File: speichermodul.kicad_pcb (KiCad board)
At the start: 2 copper layers, 100 x 160 mm, 69 parts, among them IC1 6116, J1 2PinTerminalBlocktg, J2 2PinTerminalBlocktg, J3 2PinTerminalBlocktg, P1 CONN_3X2, P8 CONN_02X10, P9 CONN_02X10, SW1 SW_PUSH-tg, SW2 SW_PUSH-tg, U1 7400, U2 74LS08, U3 74LS08, U4 74LS14, U5 74LS540, U6 74LS540

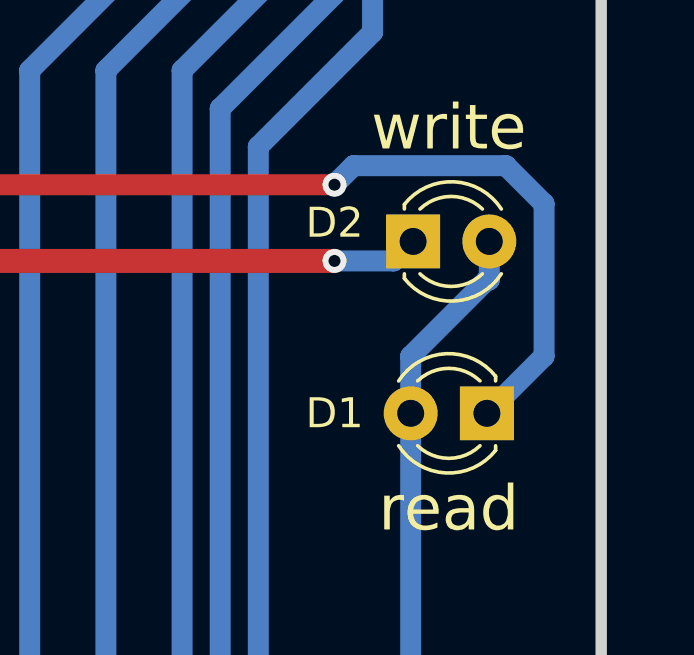
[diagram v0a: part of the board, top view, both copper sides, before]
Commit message: LEDs richtig rum gedreht
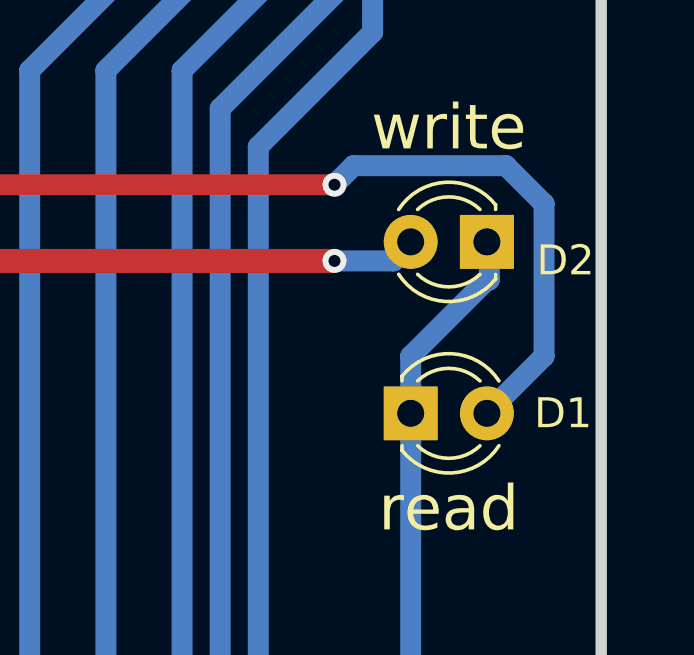
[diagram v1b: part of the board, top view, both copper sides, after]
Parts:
- moved D1 2.54 mm to (121.9, 125.7), turned to 0 degrees
- moved D2 2.46 mm to (124.5, 120.0), turned to 180 degrees
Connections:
- D1 pad 1: Net-(D1-Pad1) -> GND
- D1 pad 2: GND -> Net-(D1-Pad2)
- D2 pad 1: Net-(D2-Pad1) -> GND
- D2 pad 2: GND -> Net-(D2-Pad2)
- R7 pad 2: Net-(D1-Pad1) -> Net-(D1-Pad2)
- R8 pad 2: Net-(D2-Pad1) -> Net-(D2-Pad2)
- RP1 pad 5: (no net) -> Net-(RP1-Pad5)
- SW1 pad 2: (no net) -> Net-(SW1-Pad2)
- SW2 pad 2: (no net) -> Net-(SW2-Pad2)
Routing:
- net Net-(D1-Pad2): track 0.00 -> 65.5 mm, vias 0 -> 2
- net Net-(D1-Pad1): track 65.5 -> 0.00 mm, vias 2 -> 0
- net Net-(D2-Pad2): track 0.00 -> 57.7 mm, vias 0 -> 2
- net Net-(D2-Pad1): track 57.7 -> 0.00 mm, vias 2 -> 0

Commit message: Speichermodul weitergebaut
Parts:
- removed G***: LOGO, allBonsaiFootprintsLibs:agi5

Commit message: Speicher weitergebaut
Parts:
- removed RP2: R_PACK8BUSSED, Housings_SIP:SIP9_Housing_BigPads
- added C8: CP, Capacitor_THT:CP_Radial_D8.0mm_P2.50mm, F.Cu at (48.9, 17.8)
- added RN1: R_Network08, Resistor_THT:R_Array_SIP9, F.Cu at (62.2, 64.8)
- C1, C6, C7: footprint Capacitors_ThroughHole:C_Disc_D10.0mm_W2.5mm_P5.00mm -> Capacitor_THT:C_Disc_D10.0mm_W2.5mm_P5.00mm
- C2, C3, C4, C5: footprint tg_foodprint:yyDisc_D10.0mm_W2.5mm_P.00mm -> Capacitor_THT:C_Disc_D10.0mm_W2.5mm_P5.00mm
- D1, D2: footprint LEDs:LED_D3.0mm -> LED_THT:LED_D3.0mm
- D10, D11, D12, D13, D14, D15, D16, D17, D18, D3, D4, D5, D6, D7, D8, D9: footprint LEDs:LED_D1.8mm_W1.8mm_H2.4mm_Horizontal_O3.81mm_Z8.2mm -> LED_THT:LED_D3.0mm
- D36: footprint Diodes_ThroughHole:D_DO-41_SOD81_P10.16mm_Horizontal -> Diode_THT:D_A-405_P10.16mm_Horizontal
- IC1: footprint Housings_DIP:DIP-24_W15.24mm_Socket_LongPads -> Package_DIP:DIP-24_W15.24mm_Socket_LongPads
- J1, J2, J3: value 2PinTerminalBlocktg -> Conn_01x02; footprint 2PinTerminalBlocktg -> Connector_Molex:Molex_KK-254_AE-6410-02A_1x02_P2.54mm_Vertical
- P1: footprint Connectors_Samtec:SDL-106-X-XX_2x03 -> Connector_PinHeader_2.54mm:PinHeader_2x03_P2.54mm_Vertical
- P8: footprint Connectors_Samtec:SDL-120-X-XX_2x10 -> Connector_PinHeader_2.54mm:PinHeader_2x10_P2.54mm_Vertical
- P9: footprint Connect:IDC_Header_Straight_20pins -> Connector_PinHeader_2.54mm:PinHeader_2x10_P2.54mm_Vertical
- R1: value 1,7k -> 4k7; footprint Discret:R3 -> Resistor_THT:R_Axial_DIN0207_L6.3mm_D2.5mm_P10.16mm_Horizontal
- R10, R11, R12, R13, R14, R15, R16, R17, R18, R19, R20, R21, R22, R23, R4, R7, R8, R9: footprint Resistors_ThroughHole:R_Axial_DIN0207_L6.3mm_D2.5mm_P10.16mm_Horizontal -> Resistor_THT:R_Axial_DIN0207_L6.3mm_D2.5mm_P10.16mm_Horizontal
- R2: value 4,7k -> 4k7; footprint allBonsaiFootprintsLibs:R_Axial_DIN0207_L6.3mm_D2.5mm_P10.16mm_Horizontal -> Resistor_THT:R_Axial_DIN0207_L6.3mm_D2.5mm_P10.16mm_Horizontal
- R24, R25, R3: footprint Resistors_ThroughHole:R_Axial_DIN0309_L9.0mm_D3.2mm_P15.24mm_Horizontal -> Resistor_THT:R_Axial_DIN0207_L6.3mm_D2.5mm_P10.16mm_Horizontal
- R5: footprint allBonsaiFootprintsLibs:R_Axial_DIN0207_L6.3mm_D2.5mm_P10.16mm_Horizontal -> Resistor_THT:R_Axial_DIN0207_L6.3mm_D2.5mm_P10.16mm_Horizontal
- RP1: footprint Resistors_ThroughHole:R_Array_SIP5 -> Resistor_THT:R_Array_SIP5
- SW1, SW2: value SW_PUSH-tg -> Digitast; footprint tg_foodprint:SW_PUSH_LCD_E3_SAxxxx_tg_V2 -> bonsai:Switch_Digitast
- U1: value 7400 -> 74HC00; footprint Housings_DIP:DIP-14_W7.62mm_LongPads -> Package_DIP:DIP-14_W7.62mm_Socket_LongPads
- U2, U3: value 74LS08 -> 74HC08; footprint Housings_DIP:DIP-14_W7.62mm_LongPads -> Package_DIP:DIP-14_W7.62mm_Socket_LongPads
- U4: value 74LS14 -> 74HC14; footprint Housings_DIP:DIP-14_W7.62mm_LongPads -> Package_DIP:DIP-14_W7.62mm_Socket_LongPads
- U5: footprint Housings_DIP:DIP-20_W7.62mm_Socket_LongPads -> Package_DIP:DIP-20_W7.62mm_Socket_LongPads
- U6: footprint Housings_DIP:DIP-20_W7.62mm_LongPads -> Package_DIP:DIP-20_W7.62mm_Socket_LongPads
- moved J1 144.5 mm to (31.8, 172.1), turned to 270 degrees
- moved J3 134.2 mm to (40.6, 27.9), turned to 0 degrees
- moved J2 10.2 mm to (34.3, 161.9), turned to 90 degrees
- moved SW1 0.51 mm to (45.7, 129.5)
- moved SW2 0.13 mm to (45.1, 147.3)
- turned P9 to 270 degrees
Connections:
- IC1 pad 1: /A0 -> /A7
- IC1 pad 10: /D6 -> /D1
- IC1 pad 11: /D5 -> /D2
- IC1 pad 13: /D4 -> /D3
- IC1 pad 14: /D3 -> /D4
- IC1 pad 15: /D2 -> /D5
- IC1 pad 16: /D1 -> /D6
- IC1 pad 17: /D0 -> /D7
- IC1 pad 2: /A1 -> /A6
- IC1 pad 3: /A2 -> /A5
- IC1 pad 4: /A3 -> /A4
- IC1 pad 5: /A4 -> /A3
- IC1 pad 6: /A5 -> /A2
- IC1 pad 7: /A6 -> /A1
- IC1 pad 8: /A7 -> /A0
- IC1 pad 9: /D7 -> /D0
- J1 pad 1: GND -> WR
- J1 pad 2: VCC -> EN
- J2 pad 1: WR -> RD
- J2 pad 2: EN -> AUTO
- J3 pad 1: RD -> GND
- J3 pad 2: AUTO -> VCC
- P1 pad 2: /A8 -> /A10
- P1 pad 6: /A10 -> /A8
- P8 pad 11: /A4 -> /A3
- P8 pad 13: /A5 -> /A2
- P8 pad 15: /A6 -> /A1
- P8 pad 17: /A7 -> /A0
- P8 pad 3: /A0 -> /A7
- P8 pad 5: /A1 -> /A6
- P8 pad 7: /A2 -> /A5
- P8 pad 9: /A3 -> /A4
- P9 pad 11: /D4 -> /D3
- P9 pad 13: /D5 -> /D2
- P9 pad 15: /D6 -> /D1
- P9 pad 17: /D7 -> /D0
- P9 pad 3: /D0 -> /D7
- P9 pad 5: /D1 -> /D6
- P9 pad 7: /D2 -> /D5
- P9 pad 9: /D3 -> /D4
- U5 pad 2: /D0 -> /D7
- U5 pad 3: /D1 -> /D6
- U5 pad 4: /D2 -> /D5
- U5 pad 5: /D3 -> /D4
- U5 pad 6: /D4 -> /D3
- U5 pad 7: /D5 -> /D2
- U5 pad 8: /D6 -> /D1
- U5 pad 9: /D7 -> /D0
- U6 pad 2: /A0 -> /A7
- U6 pad 3: /A1 -> /A6
- U6 pad 4: /A2 -> /A5
- U6 pad 5: /A3 -> /A4
- U6 pad 6: /A4 -> /A3
- U6 pad 7: /A5 -> /A2
- U6 pad 8: /A6 -> /A1
- U6 pad 9: /A7 -> /A0
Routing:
- net /D7: track 105.7 -> 146.8 mm, vias 0 -> 2
- net /D0: track 146.8 -> 105.7 mm, vias 2 -> 0
- net /D6: track 107.7 -> 138.7 mm
- net /D1: track 138.7 -> 107.7 mm
- net /D5: track 111.2 -> 130.6 mm
- net /D2: track 130.6 -> 111.2 mm
- net /D4: track 115.0 -> 122.4 mm
- net /D3: track 122.4 -> 115.0 mm
- net /A7: track 85.6 -> 84.8 mm, vias 0 -> 2
- net /A0: track 84.8 -> 85.6 mm, vias 2 -> 0
- net /A5: track 84.8 -> 84.1 mm
- net /A2: track 84.1 -> 84.8 mm

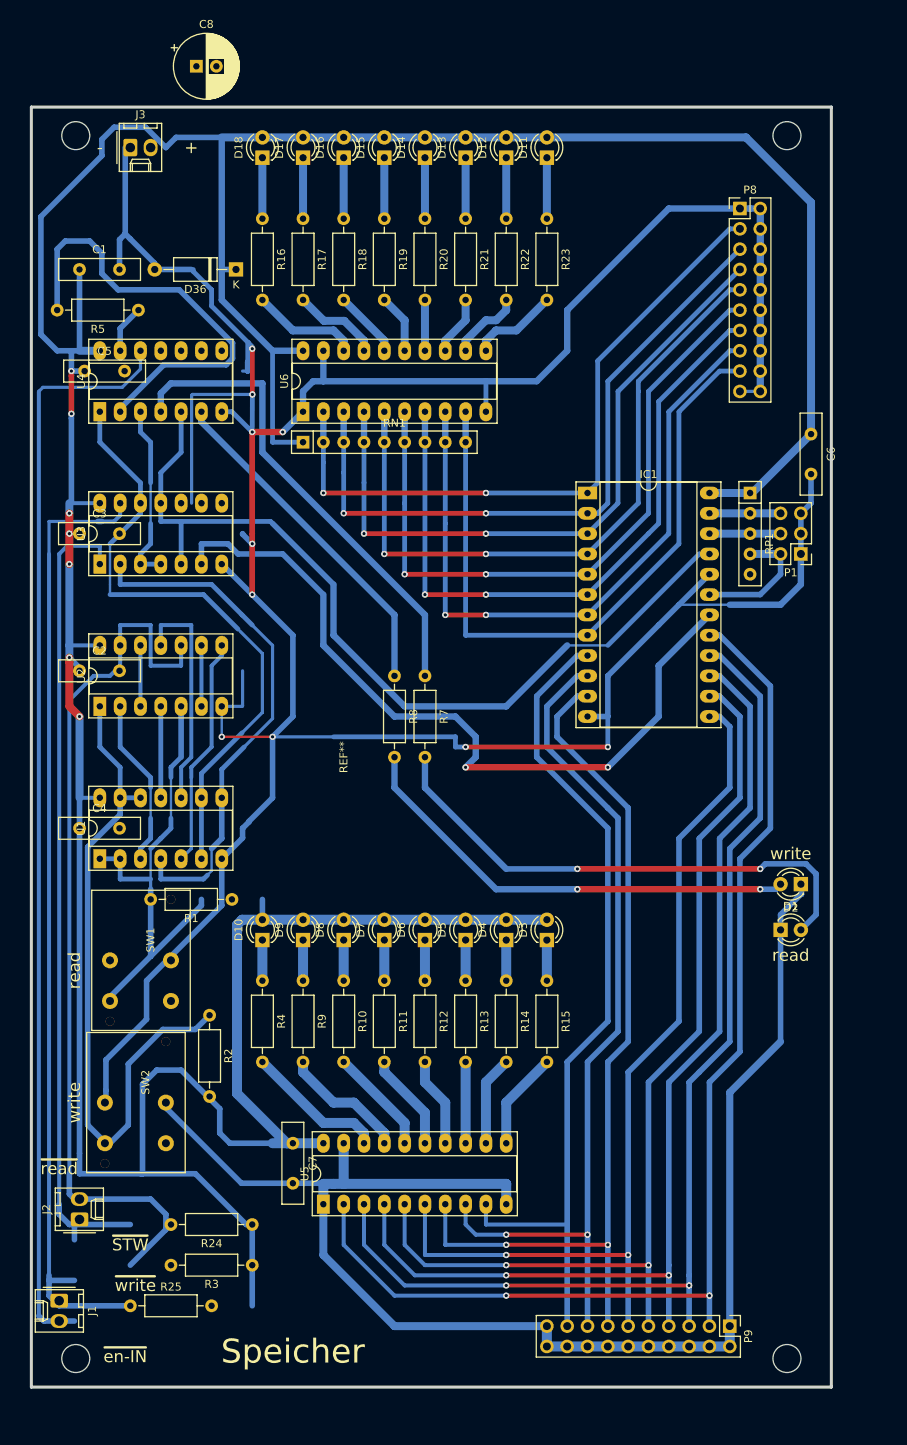
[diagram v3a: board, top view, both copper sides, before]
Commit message: Speicher Layout EinTaktReset VCO
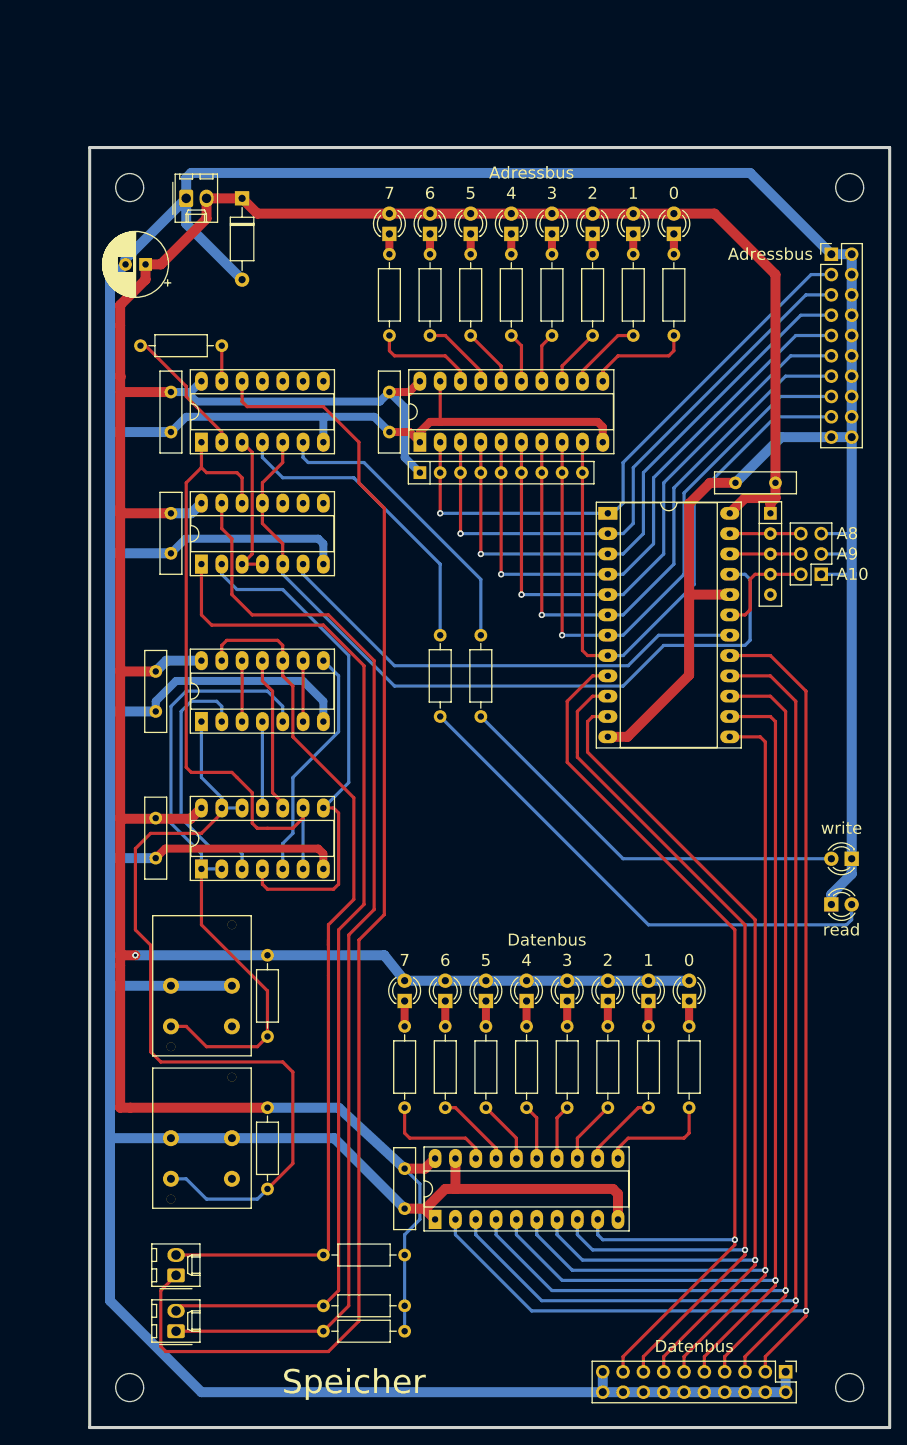
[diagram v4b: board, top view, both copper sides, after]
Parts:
- removed the REF** at (128.3, 182.9)
- added REF**: EuroBoard160mmX100mm_holes_keepout, bonsai:EuroBoard160mmX100mm_holes_keepout, F.Cu at (35.6, 27.9)
- SW1: value Digitast -> Digitast rot
- SW2: value Digitast -> Digitast grün
- moved C4 66.9 mm to (73.0, 58.5), turned to 270 degrees
- moved C1 32.6 mm to (45.7, 73.7), turned to 270 degrees
- moved C8 25.6 mm to (42.5, 42.5), turned to 180 degrees
- moved R25 24.3 mm to (64.8, 175.9)
- moved R2 22.9 mm to (57.8, 158.1), turned to 90 degrees
- moved R24 21.6 mm to (74.9, 172.7)
- moved C2 20.7 mm to (43.8, 111.8), turned to 270 degrees
- moved C3 19.7 mm to (43.8, 93.4), turned to 270 degrees
- moved D10 19.3 mm to (74.9, 134.6)
- moved D9 19.3 mm to (80.0, 134.6)
- moved D3 19.3 mm to (110.5, 134.6)
- moved D4 19.3 mm to (105.4, 134.6)
- moved D5 19.3 mm to (100.3, 134.6)
- moved D6 19.3 mm to (95.2, 134.6)
- moved D7 19.3 mm to (90.2, 134.6)
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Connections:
- net WR renamed readMem
- J1 pad 2: EN -> writeMem
- J2 pad 1: RD -> EN
- R24 pad 2: RD -> writeMem
- U3 pad 1: RD -> writeMem
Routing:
- net writeMem: track 0.00 -> 130.1 mm
- net GND: track 650.5 -> 757.3 mm, vias 10 -> 0
- net RD: track 101.7 -> 0.00 mm
- net VCC: track 501.9 -> 455.6 mm, vias 7 -> 1
- net Net-(R5-Pad2): track 55.7 -> 16.6 mm
- net Net-(IC1-Pad18): track 97.0 -> 60.9 mm, vias 2 -> 0
- net EN: track 136.4 -> 168.0 mm
- net Net-(R7-Pad1): track 60.5 -> 38.5 mm
- net Net-(R1-Pad2): track 59.4 -> 79.9 mm
- net /D0: track 105.7 -> 124.0 mm, vias 0 -> 1
- net Net-(R2-Pad1): track 84.9 -> 102.2 mm
- net /D1: track 107.7 -> 124.7 mm, vias 2 -> 1
- net readMem: track 121.4 -> 138.0 mm
- net /D2: track 111.2 -> 125.5 mm, vias 2 -> 1
- net Net-(IC1-Pad21): track 109.9 -> 95.6 mm
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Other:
- board text added: "0"
- board text added: "1"
- board text added: "2"
- board text added: "3"
- board text added: "4"
- board text added: "5"
- board text added: "6"
- board text added: "7"
- board text added: "A10"
- board text added: "A8"
- board text added: "A9"
- board text added: "Adressbus"
- board text added: "Datenbus"
- board text removed: "+"
- board text removed: "-"
- board text removed: "~STW"
- board text removed: "~en-IN"
- board text removed: "~read"
- board text removed: "~write"

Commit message: Speicher vor Tausch der Taster
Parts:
- U3: value 74HC08 -> 74HC14
- moved D1 1.27 mm to (127.0, 122.6)
- moved D2 1.27 mm to (129.5, 116.8)
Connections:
- U3 pad 10: (no net) -> VCC
- U3 pad 8: (no net) -> Net-(U3-Pad8)
- U3 pad 9: (no net) -> VCC
- U4 pad 10: (no net) -> Net-(U4-Pad10)
- U4 pad 11: (no net) -> VCC
- U4 pad 8: (no net) -> Net-(U4-Pad8)
- U4 pad 9: (no net) -> VCC
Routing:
- net VCC: track 455.6 -> 477.5 mm
- net Net-(D2-Pad2): track 51.2 -> 49.9 mm
- net Net-(D1-Pad2): track 64.4 -> 63.1 mm
- net GND: track 757.3 -> 757.9 mm
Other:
- board text added: "auto"
- board text added: "enableEin"
- board text added: "readMem"
- board text added: "writeMem"

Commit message: Speicher fertig*
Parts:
- moved R1 23.3 mm to (44.5, 148.0)
- moved R2 23.3 mm to (44.5, 139.1)
- moved SW1 19.4 mm to (57.1, 151.8)
- moved SW2 19.4 mm to (57.1, 132.7)
- moved D1 1.91 mm to (125.1, 122.6)
- moved D2 1.90 mm to (127.6, 116.8)
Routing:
- net Net-(R2-Pad1): track 102.2 -> 60.2 mm
- net Net-(R1-Pad2): track 79.9 -> 88.9 mm
- net /D6: track 141.3 -> 134.3 mm
- net /D7: track 148.2 -> 141.3 mm
- net /D4: track 127.6 -> 120.7 mm
- net /D5: track 134.5 -> 127.6 mm
- net /D3: track 120.0 -> 113.8 mm
- net /D2: track 125.5 -> 120.8 mm
- net /D1: track 124.7 -> 120.1 mm
- net /D0: track 124.0 -> 119.4 mm
- net GND: track 757.9 -> 762.5 mm
- net Net-(D2-Pad2): track 49.9 -> 48.0 mm
- net Net-(D1-Pad2): track 63.1 -> 61.2 mm
- net VCC: vias 1 -> 0
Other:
- board text added: "+"
- board text added: "-"
- board text added: "rev 2.0"
